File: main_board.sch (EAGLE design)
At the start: 60 parts, among them IC1 MBED_MICROCONTROLLER, J1 2060-402, U11 MC33887-HSOP, U13 MC33887-HSOP, U14 PCF8575PWE4, U2 SI8460AA-B-IS1, U3 MC33887-HSOP, U4 NFET-SOIC8, U5 LDO, U6 SI8460AA-B-IS1, U7 MC33887-HSOP, U8 SI8460AA-B-IS1, U9 MC33887-HSOP, X3 ENC1, X4 ENC2, X6 ENC3, X7 ENC4, X8 ENC5

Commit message: Major changes, nearly ready for first prototype
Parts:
- removed C3: 100nF, rcl:C-EUC0603K
- removed J1: 2060-402, Wago-2060-402:2060-402
- removed JP1, JP3, JP4, JP5, JP6: MOTOR, SparkFun:M023.5MM
- removed JP2: PWR, SparkFun:M023.5MM
- removed LED4: (no value), led:LEDCHIP-LED0603
- removed U14: PCF8575PWE4, pcf8575:PCF8575PWE4
- removed U4: NFET-SOIC8, SparkFun:MOSFET-NCHANNEL-SOIC8
- removed U5: LDO, SparkFun:V_REG_LDOSMD
- added BAT_12V, BAT_GND: M01_PWR, tellis2:M01_PWR
- added BAT_15V, BAT_15V_GND, M1_1, M1_10, M1_2, M1_3, M1_4, M1_5, M1_6, M1_7, M1_8, M1_9: M01_WIRE, tellis2:M01_WIRE
- added LED1, LED2, LED3: (no value), led:LEDCHIP-LED0603
- added R1: 10k, rcl:R-EU_R0603
- added R14, R7, R8, R9: 2K2, rcl:R-EU_R0603
- added U$1: V_REG_MIC2920, SparkFun-PowerIC:V_REG_MIC2920
- added U$2: MOSFET-N-SOT669, nxp_sot669:MOSFET-N-SOT669
- added U$3: D15V35F5S3, D15V35F5S3:D15V35F5S3
- added U1: PCA9555PW,118, PCA9555:PCA9555PW,118
- added X1: BALL_SENS, con-amp-micromatch:MICROMATCH-4
- added X10: IMU, con-amp-micromatch:MICROMATCH-4
- added X2: ETH, con-amp-micromatch:MICROMATCH-4
- added X5: BTNS, con-amp-micromatch:MICROMATCH-4
- added X9: COIL, con-amp-micromatch:MICROMATCH-6
- R11: value 10k -> 2K2
- R6: value 1k -> 2K2
- renumbered R19 to R2, R22 to R5, R25 to R4, R28 to R3
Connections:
- removed net EXTEND_SCL: IC1.P$10, U14.SCL
- removed net EXTEND_SDA: IC1.P$9, U14.SDA
- removed net N$11: C3.1, U5.BP
- removed net N$13: LED4.A, R6.1
- removed net N$17: R11.1, U3.EN
- new net +15V: BAT_15V.P$1, U$3.VIN
- new net BALL: U1.IO1_2, X1-2.S
- new net BTN1: U1.IO1_6, X5-2.S
- new net BTN2: U1.IO1_7, X5-4.S
- new net CHARGE: IC1.P$20, X9-4.S
- new net D+: IC1.P$31
- new net D-: IC1.P$32
- new net DONE: IC1.P$18, X9-5.S
- new net INT: IC1.P$8, R11.1, U1.!INT
- new net KICK: IC1.P$19, X9-3.S
- new net LED1: R6.2, U1.IO1_3
- new net LED2: R7.2, U1.IO1_4
- new net LED3: R8.2, U1.IO1_5
- new net N$19: X9-6.S
- new net N$2: R1.1, U3.EN
- new net N$7: LED1.A, R6.1
- new net N$8: LED2.A, R7.1
- new net N$9: LED3.A, R8.1
- new net RD+: IC1.P$35, X2-2.S
- new net RD-: IC1.P$36, X2-1.S
- new net SCL: IC1.P$10, R9.1, U1.SCL, X10-3.S
- new net SDA: IC1.P$9, R14.1, U1.SDA, X10-4.S
- new net TD+: IC1.P$33, X2-4.S
- new net TD-: IC1.P$34, X2-3.S
- net +12V: now also U$1.IN; no longer U5.EN, U5.IN
- net +3V3: now also R11.2, R14.2, R9.2, U1.VDD, X10-1.S; no longer U14.VCC
- net +5V: now also R1.2, U$1.OUT; no longer R11.2, R6.2, U5.OUT
- net DIR1_1: now also U1.IO0_1, U2.A4; no longer U14.P00, U2.A2
- net DIR1_1_D: now also U2.B4; no longer U2.B2
- net DIR1_2: now also U1.IO0_0, U2.A5; no longer U14.P01, U2.A3
- net DIR1_2_D: now also U2.B5; no longer U2.B3
- net DIR2_1: now also U1.IO0_3, U2.A1; no longer U14.P02, U2.A5
- net DIR2_1_D: now also U2.B1; no longer U2.B5
- net DIR2_2: now also U1.IO0_2, U2.A2; no longer U14.P03, U2.A6
- net DIR2_2_D: now also U2.B2; no longer U2.B6
- net DIR3_1: now also U1.IO0_5, U6.A4; no longer U14.P04, U6.A2
- net DIR3_1_D: now also U6.B4; no longer U6.B2
- net DIR3_2: now also U1.IO0_4, U6.A5; no longer U14.P05, U6.A3
- net DIR3_2_D: now also U6.B5; no longer U6.B3
- net DIR4_1: now also U1.IO0_7, U6.A1; no longer U14.P06, U6.A5
- net DIR4_1_D: now also U6.B1; no longer U6.B5
- net DIR4_2: now also U1.IO0_6, U6.A2; no longer U14.P07, U6.A6
- net DIR4_2_D: now also U6.B2; no longer U6.B6
- net DIR5_1: now also U1.IO1_0, U8.A1; no longer U14.P10, U8.A2
- net DIR5_1_D: now also U8.B1; no longer U8.B2
- net DIR5_2: now also U1.IO1_1, U8.A2; no longer U14.P11, U8.A3
- net DIR5_2_D: now also U8.B2; no longer U8.B3
- net ENC1A: now also IC1.P$5; no longer IC1.P$8
- net ENC1B: now also IC1.P$6; no longer IC1.P$11
- net ENC2A: now also IC1.P$7; no longer IC1.P$12
- net ENC2B: now also IC1.P$11; no longer IC1.P$15
- net ENC3A: now also IC1.P$12; no longer IC1.P$16
- net ENC3B: now also IC1.P$13; no longer IC1.P$17
- net ENC4A: now also IC1.P$14; no longer IC1.P$18
- net ENC4B: now also IC1.P$15; no longer IC1.P$26
- net ENC5A: now also IC1.P$16; no longer IC1.P$27
- net ENC5B: now also IC1.P$17; no longer IC1.P$28
- net GND: now also BAT_15V_GND.P$1, LED1.C, LED2.C, LED3.C, U$3.GND, U1.A0, U1.A1, U1.A2, U1.VSS, X1-1.S, X10-2.S, X5-1.S, X5-3.S, X9-1.S; no longer U14.A0, U14.A1, U14.A2, U14.GND
- net GNDA: now also U$1.GND, U$2.S; no longer C3.2, LED4.C, U4.S@1, U4.S@2, U4.S@3, U5.GND
- net N$20: now also U$2.G; no longer U4.G
- net N$21: now also BAT_GND.P$1, U$2.D; no longer JP2.1, U4.D@1, U4.D@2, U4.D@3, U4.D@4
- net N$23: now also M1_1.P$1; no longer JP1.2
- net N$25: now also M1_2.P$1; no longer JP1.1
- net N$30: now also BAT_12V.P$1; no longer JP2.2
- net N$34: now also M1_3.P$1; no longer JP3.2
- net N$35: now also M1_4.P$1; no longer JP3.1
- net N$39: now also M1_5.P$1; no longer JP4.2
- net N$40: now also M1_6.P$1; no longer JP4.1
- net N$44: now also M1_7.P$1; no longer JP5.2
- net N$45: now also M1_8.P$1; no longer JP5.1
- net N$49: now also M1_9.P$1; no longer JP6.2
- net N$50: now also M1_10.P$1; no longer JP6.1
- net PWM1: now also IC1.P$25, U2.A6; no longer IC1.P$21, U2.A1
- net PWM1_D: now also U2.B6; no longer U2.B1
- net PWM2: now also IC1.P$24, U2.A3; no longer IC1.P$22, U2.A4
- net PWM2_D: now also U2.B3; no longer U2.B4
- net PWM3: now also U6.A6; no longer U6.A1
- net PWM3_D: now also U6.B6; no longer U6.B1
- net PWM4: now also IC1.P$22, U6.A3; no longer IC1.P$24, U6.A4
- net PWM4_D: now also U6.B3; no longer U6.B4
- net PWM5: now also IC1.P$21, U8.A3; no longer IC1.P$25, U8.A1
- net PWM5_D: now also U8.B3; no longer U8.B1
- net VCC: now also U$3.VOUT, X1-3.S, X9-2.S
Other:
- moved on the sheet: R11, R6

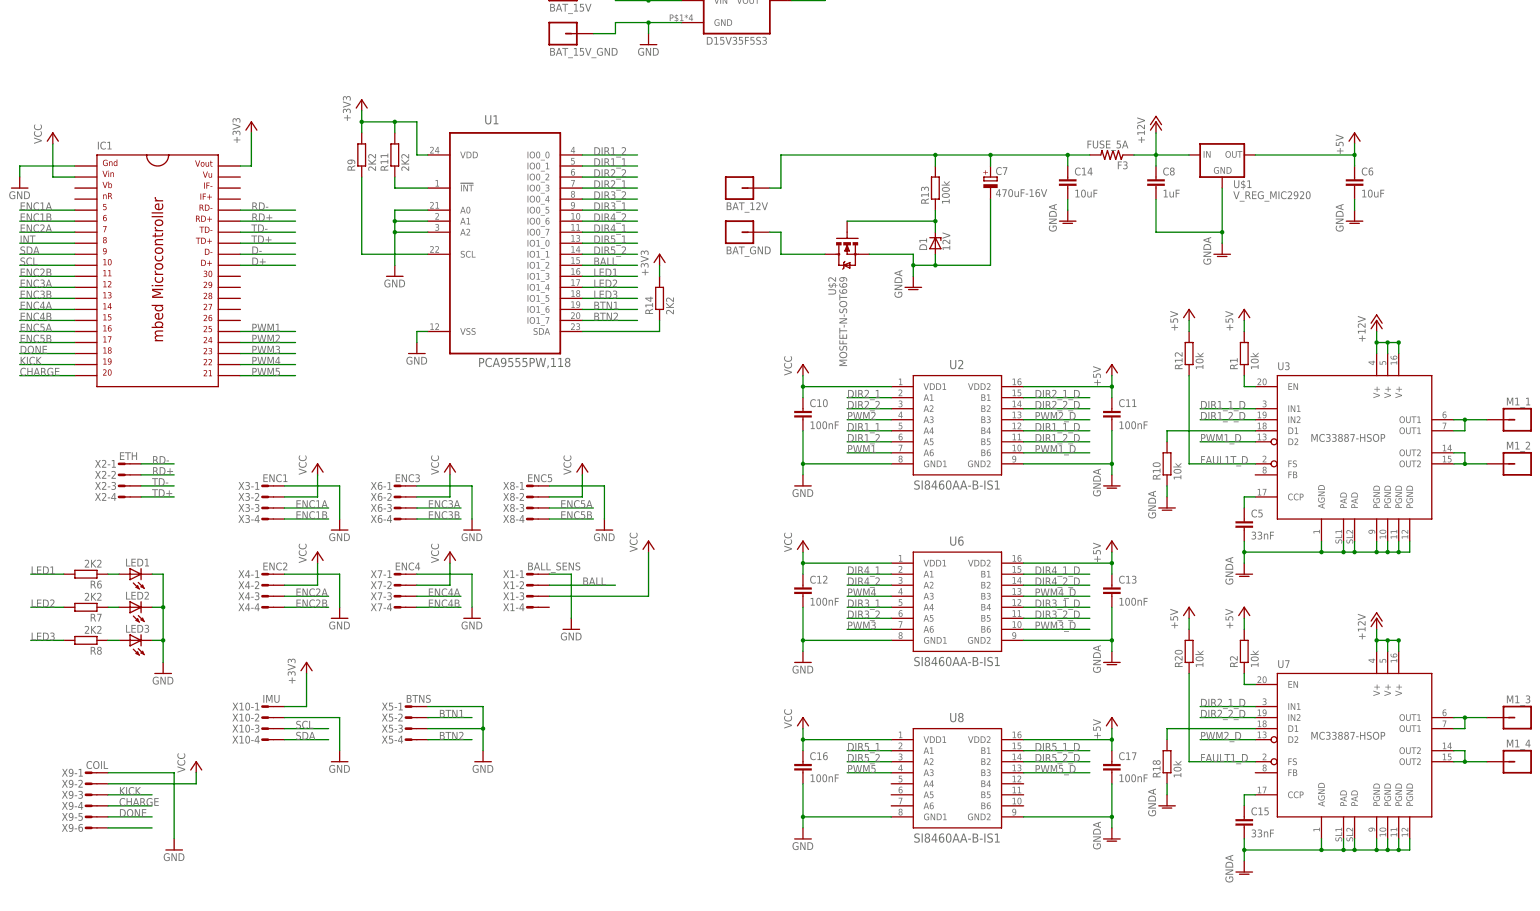
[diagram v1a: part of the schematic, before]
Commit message: Improved board layout
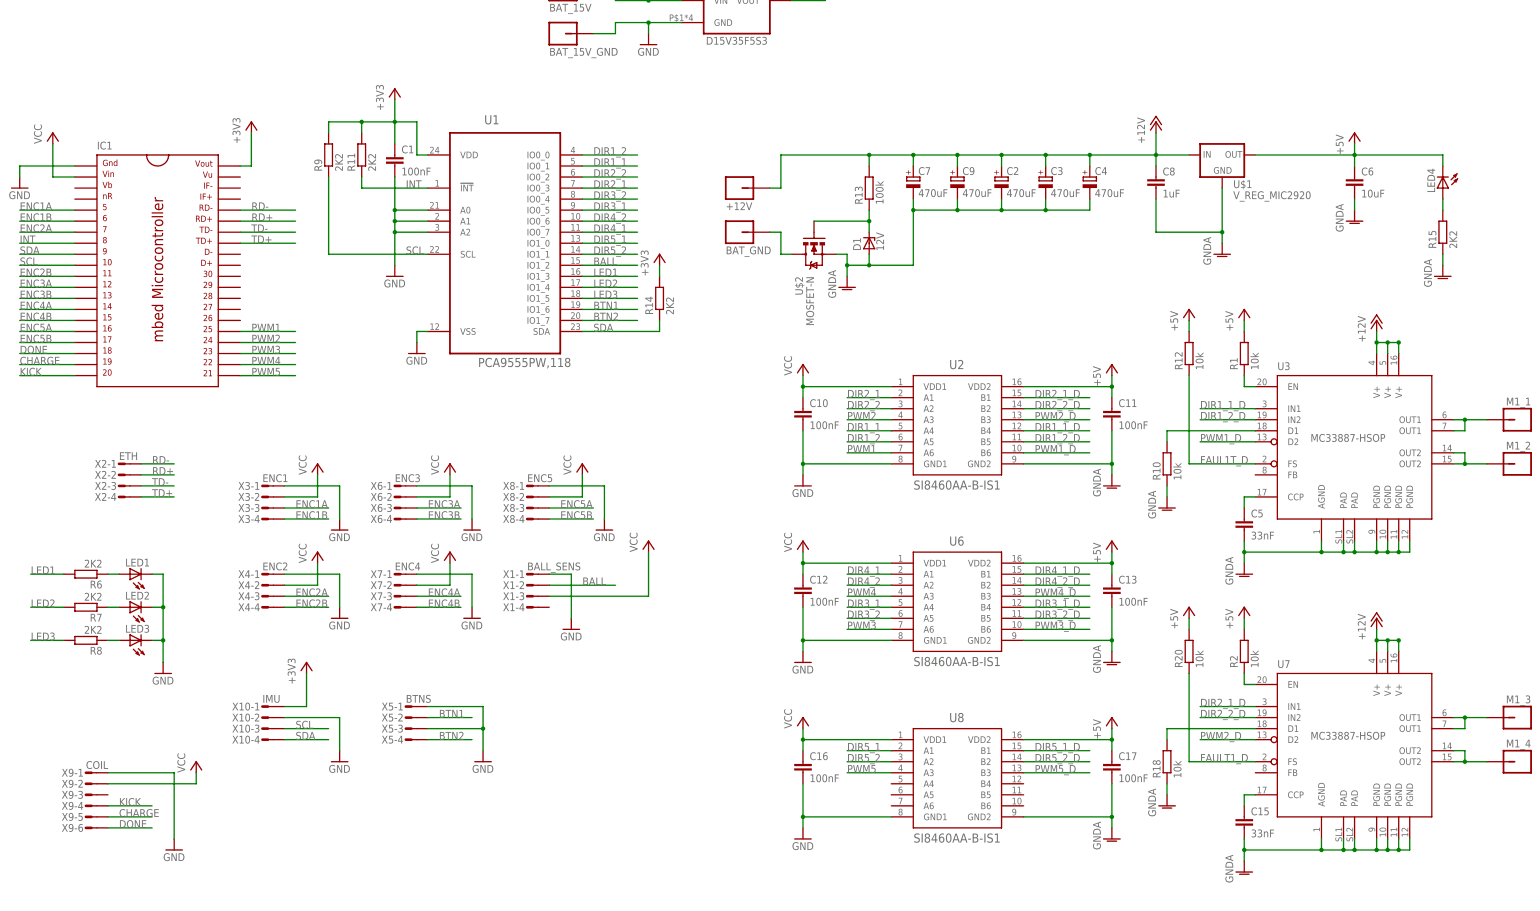
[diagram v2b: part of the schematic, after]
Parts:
- removed C14: 10uF, rcl:C-EUC1206K
- removed F3: FUSE_5A, rcl:R-US_R1206
- added C1: 100nF, rcl:C-EUC0603K
- added C2, C3, C4, C9: 470uF, rcl:CPOL-EUE3.5-8
- added LED4: (no value), led:LEDCHIP-LED0603
- added R15: 2K2, rcl:R-EU_R0603
- C7: value 470uF-16V -> 470uF
- U$2: value MOSFET-N-SOT669 -> MOSFET-N
- renumbered BAT_12V to +12V
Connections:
- removed net D+: IC1.P$31
- removed net D-: IC1.P$32
- removed net N$19: X9-6.S
- removed net N$30: +12V.P$1, C14.1, C7.+, F3.2, R13.2
- new net N$10: LED4.A, R15.2
- net +12V: now also +12V.P$1, C2.+, C3.+, C4.+, C7.+, C9.+, R13.2; no longer F3.1
- net +3V3: now also C1.1
- net +5V: now also LED4.C
- net CHARGE: now also IC1.P$19, X9-5.S; no longer IC1.P$20, X9-4.S
- net DONE: now also X9-6.S; no longer X9-5.S
- net GND: now also C1.2
- net GNDA: now also C2.-, C3.-, C4.-, C9.-, R15.1; no longer C14.2
- net KICK: now also IC1.P$20, X9-4.S; no longer IC1.P$19, X9-3.S
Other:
- moved on the sheet: C7, D1, R11, R13, R9, U$2

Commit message: Added capacitor to buttons, switched IMU and buttons connector positions, moved voltage regulator to better position, connected IMU connector to second I2C pins added pull-down resistors to PWM pins, added pull-up resitor to kick pin, added pull-down resistor to charge pin, made wire holes a bit bigger
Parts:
- added C14, C18: 100nF, rcl:C-EUC0603K
- added R16, R17, R19, R22, R25, R28, R30: 10k, rcl:R-EU_R0603
- added R31, R32: 2K2, rcl:R-EU_R0603
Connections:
- new net SCL2: IC1.P$27, R32.1, X10-3.S
- new net SDA2: IC1.P$28, R31.1, X10-4.S
- net +3V3: now also R31.2, R32.2
- net BTN1: now also C14.1
- net BTN2: now also C18.1
- net CHARGE: now also R17.2
- net GND: now also C14.2, C18.2, R17.1, R19.1, R22.1, R25.1, R28.1, R30.1
- net KICK: now also R16.1
- net PWM1: now also R30.2
- net PWM2: now also R28.2
- net PWM3: now also R25.2
- net PWM4: now also R22.2
- net PWM5: now also R19.2
- net SCL: no longer X10-3.S
- net SDA: no longer X10-4.S
- net VCC: now also R16.2
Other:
- moved on the sheet: +12V, BAT_GND, C1, C2, C3, C4, C6, C7, C8, C9, D1, LED4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

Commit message: Added two more LEDs to IO extender pins, connected buttons directly to mbed
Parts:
- added LED5, LED_5V: (no value), led:LEDCHIP-LED0603
- added R33, R34: 2K2, rcl:R-EU_R0603
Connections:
- new net LED4: R33.2, U1.IO1_6
- new net LED5: R34.2, U1.IO1_7
- new net N$11: LED4.A, R33.1
- new net N$12: LED5.A, R34.1
- net +5V: now also LED_5V.C; no longer LED4.C
- net BTN1: now also IC1.P$30; no longer U1.IO1_6
- net BTN2: now also IC1.P$29; no longer U1.IO1_7
- net GND: now also LED4.C, LED5.C
- net N$10: now also LED_5V.A; no longer LED4.A
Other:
- moved on the sheet: LED4
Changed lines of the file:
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@@
 <part name="C4" library="rcl" deviceset="CPOL-EU" device="E3.5-8" value="470uF"/>
 <part name="C9" library="rcl" deviceset="CPOL-EU" device="E3.5-8" value="470uF"/>
-<part name="LED4" library="led" deviceset="LED" device="CHIP-LED0603"/>
+<part name="LED_5V" library="led" deviceset="LED" device="CHIP-LED0603"/>
 <part name="R15" library="rcl" deviceset="R-EU_" device="R0603" value="2K2"/>
 <part name="GND16" library="supply1" deviceset="GNDA" device=""/>
@@
 <part name="R32" library="rcl" deviceset="R-EU_" device="R0603" value="2K2"/>
 <part name="+3V3" library="supply1" deviceset="+3V3" device=""/>
+<part name="LED4" library="led" deviceset="LED" device="CHIP-LED0603"/>
+<part name="LED5" library="led" deviceset="LED" device="CHIP-LED0603"/>
+<part name="R33" library="rcl" deviceset="R-EU_" device="R0603" value="2K2"/>
+<part name="R34" library="rcl" deviceset="R-EU_" device="R0603" value="2K2"/>
 </parts>
 <sheets>
@@
 <instance part="LED2" gate="G$1" x="-45.72" y="20.32" rot="R90"/>
 <instance part="LED3" gate="G$1" x="-45.72" y="12.7" rot="R90"/>
-<instance part="GND4" gate="1" x="-38.1" y="5.08"/>
+<instance part="GND4" gate="1" x="-38.1" y="-7.62"/>
 <instance part="R6" gate="G$1" x="-55.88" y="27.94" rot="R180"/>
 <instance part="R7" gate="G$1" x="-55.88" y="20.32" rot="R180"/>
@@
 <instance part="C4" gate="G$1" x="200.66" y="124.46"/>
 <instance part="C9" gate="G$1" x="170.18" y="124.46"/>
-<instance part="LED4" gate="G$1" x="281.94" y="121.92" rot="R180"/>
+<instance part="LED_5V" gate="G$1" x="281.94" y="121.92" rot="R180"/>
 <instance part="R15" gate="G$1" x="281.94" y="111.76" rot="R90"/>
 <instance part="GND16" gate="1" x="281.94" y="101.6"/>
@@
 <instance part="R32" gate="G$1" x="7.62" y="99.06" rot="R90"/>
 <instance part="+3V3" gate="G$1" x="0" y="111.76"/>
+<instance part="LED4" gate="G$1" x="-45.72" y="5.08" rot="R90"/>
+<instance part="LED5" gate="G$1" x="-45.72" y="-2.54" rot="R90"/>
+<instance part="R33" gate="G$1" x="-55.88" y="5.08" rot="R180"/>
+<instance part="R34" gate="G$1" x="-55.88" y="-2.54" rot="R180"/>
 </instances>
 <busses>
@@
 <pinref part="GND4" gate="1" pin="GND"/>
 <wire x1="-40.64" y1="12.7" x2="-38.1" y2="12.7" width="0.1524" layer="91"/>
-<wire x1="-38.1" y1="12.7" x2="-38.1" y2="7.62" width="0.1524" layer="91"/>
+<wire x1="-38.1" y1="12.7" x2="-38.1" y2="5.08" width="0.1524" layer="91"/>
 <pinref part="LED2" gate="G$1" pin="C"/>
+<wire x1="-38.1" y1="5.08" x2="-38.1" y2="-2.54" width="0.1524" layer="91"/>
+<wire x1="-38.1" y1="-2.54" x2="-38.1" y2="-5.08" width="0.1524" layer="91"/>
 <wire x1="-40.64" y1="20.32" x2="-38.1" y2="20.32" width="0.1524" layer="91"/>
 <wire x1="-38.1" y1="20.32" x2="-38.1" y2="12.7" width="0.1524" layer="91"/>
@@
 <junction x="-38.1" y="20.32"/>
 <junction x="-38.1" y="12.7"/>
+<pinref part="LED4" gate="G$1" pin="C"/>
+<wire x1="-40.64" y1="5.08" x2="-38.1" y2="5.08" width="0.1524" layer="91"/>
+<pinref part="LED5" gate="G$1" pin="C"/>
+<wire x1="-40.64" y1="-2.54" x2="-38.1" y2="-2.54" width="0.1524" layer="91"/>
+<junction x="-38.1" y="-2.54"/>
+<junction x="-38.1" y="5.08"/>
 </segment>
 <segment>
@@
 <pinref part="U$1" gate="G$1" pin="OUT"/>
 <wire x1="261.62" y1="129.54" x2="281.94" y2="129.54" width="0.1524" layer="91"/>
-<pinref part="LED4" gate="G$1" pin="C"/>
+<pinref part="LED_5V" gate="G$1" pin="C"/>
 <wire x1="281.94" y1="129.54" x2="281.94" y2="127" width="0.1524" layer="91"/>
 </segment>
@@
 <net name="BTN2" class="0">
 <segment>
-<pinref part="U1" gate="A" pin="IO1_7"/>
-<wire x1="91.44" y1="88.9" x2="104.14" y2="88.9" width="0.1524" layer="91"/>
-<label x="93.98" y="88.9" size="1.778" layer="95"/>
-</segment>
-<segment>
 <pinref part="X5" gate="-4" pin="S"/>
 <wire x1="22.86" y1="-10.16" x2="33.02" y2="-10.16" width="0.1524" layer="91"/>
@@
 <wire x1="33.02" y1="-10.16" x2="33.02" y2="-12.7" width="0.1524" layer="91"/>
 </segment>
+<segment>
+<pinref part="IC1" gate="G$1" pin="P$29"/>
+<wire x1="-20.32" y1="93.98" x2="-7.62" y2="93.98" width="0.1524" layer="91"/>
+<label x="-17.78" y="93.98" size="1.778" layer="95"/>
+</segment>
 </net>
 <net name="BTN1" class="0">
-<segment>
-<pinref part="U1" gate="A" pin="IO1_6"/>
-<wire x1="91.44" y1="91.44" x2="104.14" y2="91.44" width="0.1524" layer="91"/>
-<label x="93.98" y="91.44" size="1.778" layer="95"/>
-</segment>
 <segment>
 <pinref part="X5" gate="-2" pin="S"/>
@@
 <wire x1="43.18" y1="-5.08" x2="43.18" y2="-12.7" width="0.1524" layer="91"/>
 </segment>
+<segment>
+<pinref part="IC1" gate="G$1" pin="P$30"/>
+<wire x1="-20.32" y1="96.52" x2="-7.62" y2="96.52" width="0.1524" layer="91"/>
+<label x="-17.78" y="96.52" size="1.778" layer="95"/>
+</segment>
 </net>
 <net name="LED3" class="0">
@@
 <net name="N$10" class="0">
 <segment>
-<pinref part="LED4" gate="G$1" pin="A"/>
+<pinref part="LED_5V" gate="G$1" pin="A"/>
 <pinref part="R15" gate="G$1" pin="2"/>
 <wire x1="281.94" y1="116.84" x2="281.94" y2="119.38" width="0.1524" layer="91"/>
@@
 </segment>
 </net>
+<net name="LED4" class="0">
+<segment>
+<pinref part="U1" gate="A" pin="IO1_6"/>
+<wire x1="91.44" y1="91.44" x2="104.14" y2="91.44" width="0.1524" layer="91"/>
+<label x="93.98" y="91.44" size="1.778" layer="95"/>
+</segment>
+<segment>
+<pinref part="R33" gate="G$1" pin="2"/>
+<wire x1="-60.96" y1="5.08" x2="-68.58" y2="5.08" width="0.1524" layer="91"/>
+<label x="-68.58" y="5.08" size="1.778" layer="95"/>
+</segment>
+</net>
+<net name="LED5" class="0">
+<segment>
+<pinref part="U1" gate="A" pin="IO1_7"/>
+<wire x1="91.44" y1="88.9" x2="104.14" y2="88.9" width="0.1524" layer="91"/>
+<label x="93.98" y="88.9" size="1.778" layer="95"/>
+</segment>
+<segment>
+<pinref part="R34" gate="G$1" pin="2"/>
+<wire x1="-60.96" y1="-2.54" x2="-68.58" y2="-2.54" width="0.1524" layer="91"/>
+<label x="-68.58" y="-2.54" size="1.778" layer="95"/>
+</segment>
+</net>
+<net name="N$11" class="0">
+<segment>
+<pinref part="R33" gate="G$1" pin="1"/>
+<pinref part="LED4" gate="G$1" pin="A"/>
+<wire x1="-50.8" y1="5.08" x2="-48.26" y2="5.08" width="0.1524" layer="91"/>
+</segment>
+</net>
+<net name="N$12" class="0">
+<segment>
+<pinref part="R34" gate="G$1" pin="1"/>
+<pinref part="LED5" gate="G$1" pin="A"/>
+<wire x1="-50.8" y1="-2.54" x2="-48.26" y2="-2.54" width="0.1524" layer="91"/>
+</segment>
+</net>
